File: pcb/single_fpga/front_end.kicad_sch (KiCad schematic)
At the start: 12 parts, among them J1 Main Power Input, J2 AXK5S80347YG, U1 TLV62569DBV

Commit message: Made CON1-4 separate parts. Fixed board-to-board connectors.
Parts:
- J2: value AXK5S80347YG -> AXK5S80337YG; footprint AXK5S80347YG:CONN80_AXK5S80347YG_PAN -> AXK5S80337YG:AXK5S80337YG; symbol AXK5S80347YG:AXK5S80347YG -> AXK5S80337YG:AXK5S80337YG
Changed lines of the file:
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@@
 	)
 	(symbol
-		(lib_id "AXK5S80347YG:AXK5S80347YG")
+		(lib_id "AXK5S80337YG:AXK5S80337YG")
 		(at 219.71 39.37 0)
 		(unit 1)
@@
 			)
 		)
-		(property "Value" "AXK5S80347YG"
+		(property "Value" "AXK5S80337YG"
 			(at 230.378 36.068 0)
 			(show_name no)
@@
 			)
 		)
-		(property "Footprint" "AXK5S80347YG:CONN80_AXK5S80347YG_PAN"
+		(property "Footprint" "AXK5S80337YG:AXK5S80337YG"
 			(at 219.71 39.37 0)
 			(hide yes)
@@
 			)
 		)
-		(property "Datasheet" "https://www.mouser.com/catalog/specsheets/AXK.pdf"
+		(property "Datasheet" "datasheets/con_eng_p5k.pdf"
 			(at 219.71 39.37 0)
 			(hide yes)
@@
 			)
 		)
-		(property "Description" "Panasonic AXK580137YG -- P5K series 0.5mm-pitch 80-pin board-to-board SOCKET, module side (confirmed on the ALINX AC7200 module; mates with the carrier board's own AXK680337YG header -- see ../../AC7200/AC7200_README.md). Real dimensions from Panasonic/Mouser's own P5K/P5KS catalog PDF (mouser.com/catalog/specsheets/AXK.pdf), read directly: body 23.20 x 19.50mm (A x B, same as the header), 0.5mm pitch, 40 pins/row x 2 rows staggered by 0.25mm (half pitch), pad 0.25 x 0.75mm, total footprint span 6.80mm (wider than the header's 5.60mm -- read directly off the Socket's own land-pattern drawing, not assumed equal to the header). Part number CONFIRMED, not assumed: the AC7200 module's own STEP model (AC7200.3.0.stp) names this connector 'AXK680137YG', which doesn't decode against Panasonic's real P5K part-number table (leading digit 6 = Header selector, but mated-height digit 1 is documented Socket-only) -- flagged as a likely STEP-model typo when this part was first built. ALINX's own real schematic (docs/AC7200_Schematic.pdf, page 12 'AC7200 CONNECTOR') settles it: all 4 connector reference labels explicitly read 'AXK580137YG', confirming the STEP model's name was wrong and this (leading digit 5) is the real part. All 320 CON1-4 signal-pin assignments in ../../AC7200/KiCad/AC7200.kicad_sym were also cross-checked pin-by-pin against that same real schematic -- exact match, no discrepancies. Pin numbering on THIS standalone connector symbol (1-80 sequential by row) is still an ASSUMED convention, matching the header's own same assumption -- the real schematic only labels FPGA bank/ball nets on CON1-4, not this connector's own physical pin-to-number layout, so it wasn't independently verifiable against a real pin-1 diagram in the catalog either."
+		(property "Description" "Panasonic AXK5S80337YG -- P5KS 0.5mm-pitch 80-pin board-to-board SOCKET, 7.0/8.0/9.0mm mated height, with positioning bosses. Mates AXK6S80637YG at 9.0mm."
 			(at 219.71 39.37 0)
 			(hide yes)

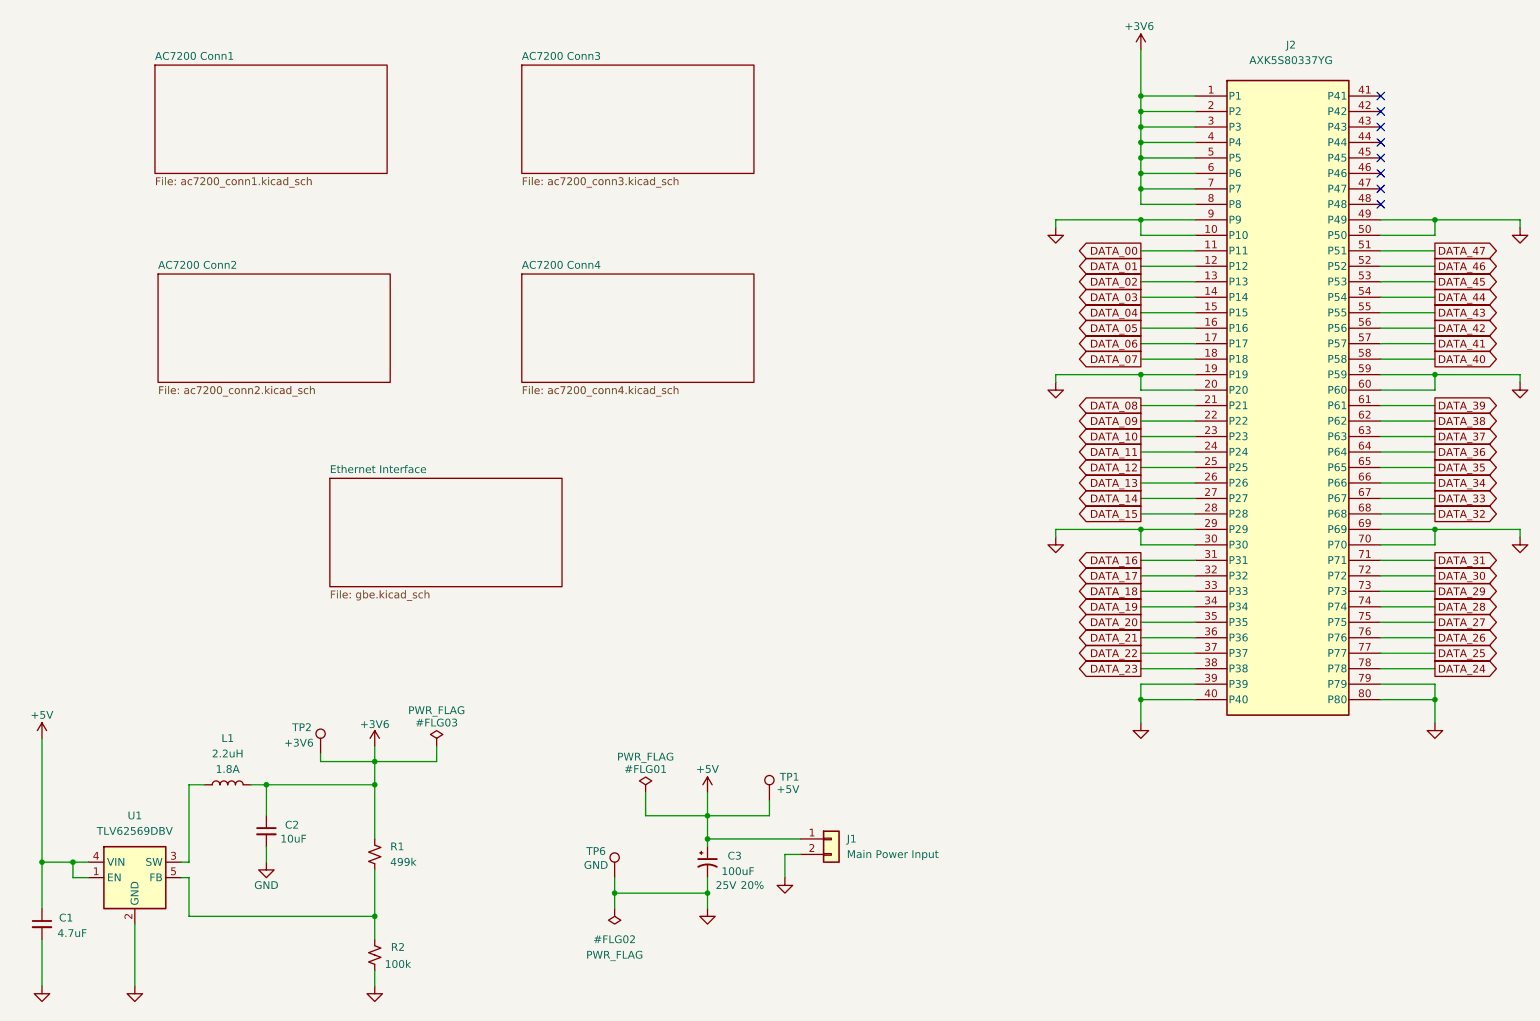
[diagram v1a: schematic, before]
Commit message: Fixed power rails. Fixed C3. Changed U4. ERC FEB.
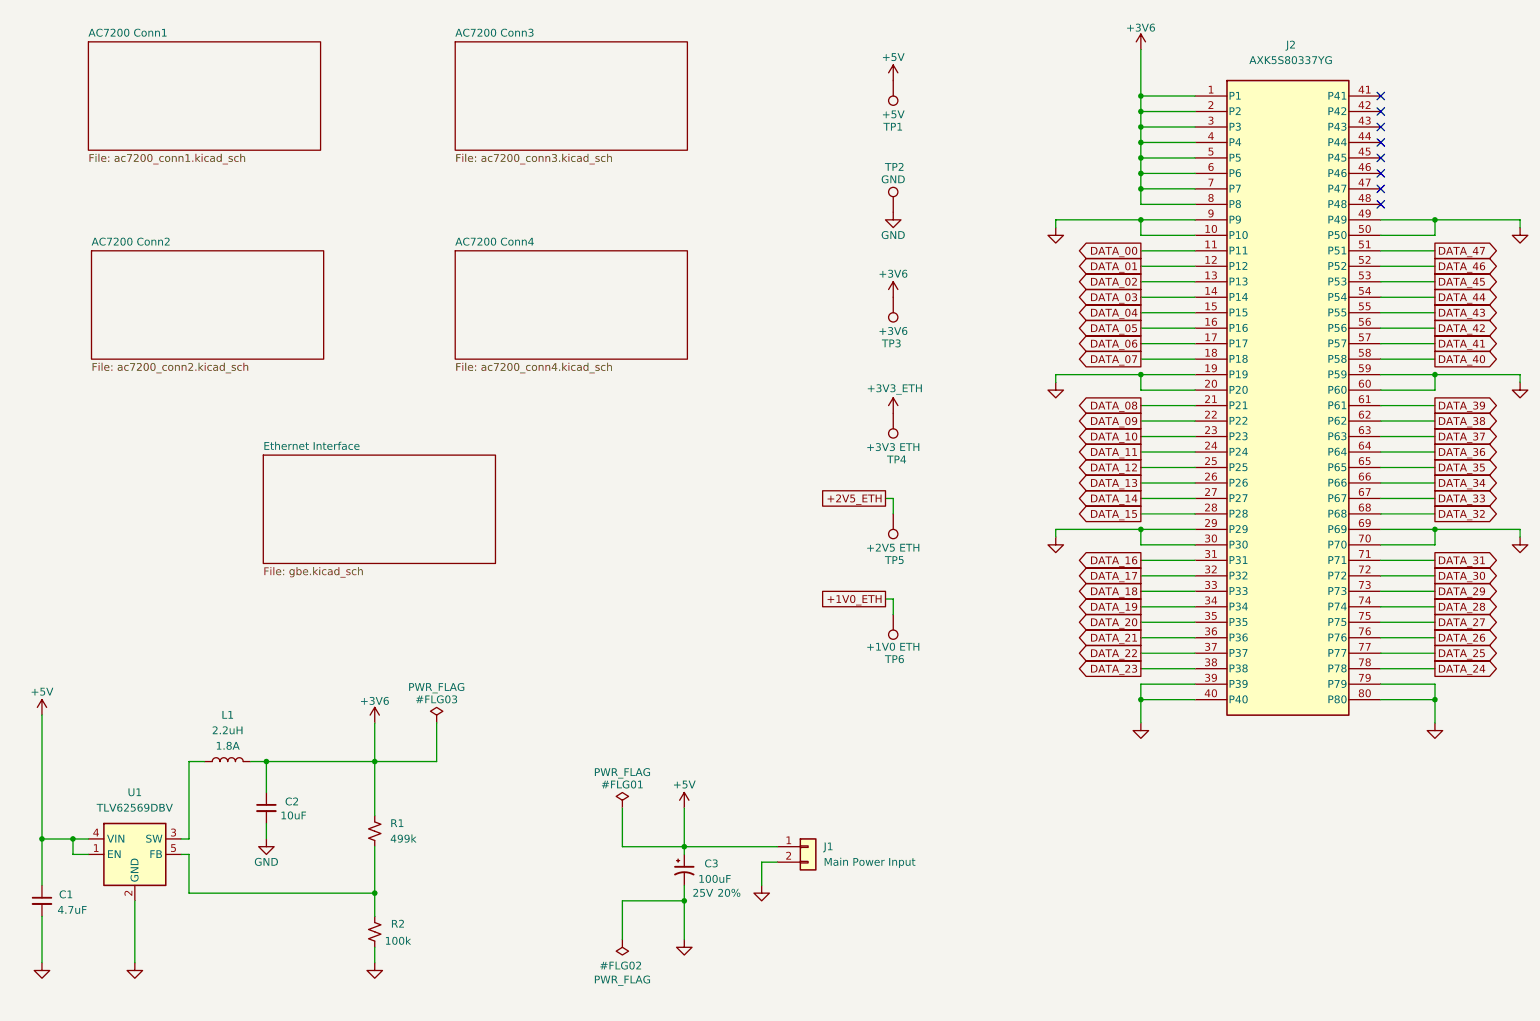
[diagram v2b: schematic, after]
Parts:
- added TP3: +3V6, TestPoint:TestPoint_THTPad_D2.0mm_Drill1.0mm, symbol Connector:TestPoint
- added TP4: +3V3 ETH, TestPoint:TestPoint_THTPad_D2.0mm_Drill1.0mm, symbol Connector:TestPoint
- added TP5: +2V5 ETH, TestPoint:TestPoint_THTPad_D2.0mm_Drill1.0mm, symbol Connector:TestPoint
- C3: footprint PCM_SparkFun-Capacitor:Panasonic_D -> Capacitor_SMD:CP_Elec_6.3x5.8
- TP2: value +3V6 -> GND
- TP6: value GND -> +1V0 ETH
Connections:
- net +3V6: now also TP3.1; no longer TP2.1
- net GND: now also TP2.1; no longer TP6.1
- new net +1V0_ETH: TP6.1
- new net +2V5_ETH: TP5.1
- new net +3V3_ETH: TP4.1
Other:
- moved on the sheet: C1, C2, C3, J1, L1, R1, R2, U1

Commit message: Routed. Almost DRC-clean.
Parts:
- C1: footprint SparkFun-Capacitor:C_1206_3216Metric -> Capacitor_SMD:C_0805_2012Metric; Manufacturer (none) -> Murata; PROD_ID CAP-10300 -> (none); Part Number (none) -> GRM21BR71A475KA73L; Temperature Coefficient Y5V -> X7R; Tolerance (none) -> 10%; Voltage (none) -> 10V
- C2: footprint PCM_SparkFun-Capacitor:C_0805_2012Metric -> Capacitor_SMD:C_0805_2012Metric; Manufacturer (none) -> Murata; PROD_ID CAP-14259 -> (none); Part Number (none) -> GRM21BR71A106KE51L; Temperature Coefficient (none) -> X7R; Tolerance (none) -> 10%; Voltage (none) -> 10V
- L1: footprint Inductor_SMD:L_Taiyo-Yuden_NR-20xx_HandSoldering -> Inductor_SMD:L_Murata_DFE201610P; Manufacturer TDK -> Murata; Manufacturer 2 Taiyo Yuden -> (none); Part Number 2 NRH2412T2R2MNGH -> (none)
- R1, R2: footprint PCM_SparkFun-Resistor:R_0603_1608Metric -> Resistor_SMD:R_0603_1608Metric; PROD_ID RES-07828 -> (none); Tolerance (none) -> 1%
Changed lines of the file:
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@@
 			)
 		)
-		(property "Footprint" "SparkFun-Capacitor:C_1206_3216Metric"
+		(property "Footprint" "Capacitor_SMD:C_0805_2012Metric"
 			(at 25.4 185.42 0)
 			(hide yes)
@@
 			)
 		)
-		(property "Datasheet" "https://search.kemet.com/download/datasheet/C1206C475Z4VAC7800"
+		(property "Datasheet" ""
 			(at 25.4 190.5 0)
 			(hide yes)
@@
 			)
 		)
-		(property "PROD_ID" "CAP-10300"
-			(at 24.13 187.96 0)
-			(hide yes)
-			(show_name no)
-			(do_not_autoplace no)
-			(effects
-				(font
-					(size 1.27 1.27)
-				)
-			)
-		)
-		(property "Voltage" ""
+		(property "Voltage" "10V"
 			(at 27.94 175.2662 0)
 			(hide yes)
@@
 			)
 		)
-		(property "Tolerance" ""
+		(property "Tolerance" "10%"
 			(at 27.94 177.8062 0)
 			(hide yes)
@@
 			)
 		)
-		(property "Temperature Coefficient" "Y5V"
+		(property "Temperature Coefficient" "X7R"
 			(at 26.162 195.834 0)
+			(hide yes)
+			(show_name no)
+			(do_not_autoplace no)
+			(effects
+				(font
+					(size 1.27 1.27)
+				)
+			)
+		)
+		(property "Manufacturer" "Murata"
+			(at 25.4 190.5 0)
+			(hide yes)
+			(show_name no)
+			(do_not_autoplace no)
+			(effects
+				(font
+					(size 1.27 1.27)
+				)
+			)
+		)
+		(property "Part Number" "GRM21BR71A475KA73L"
+			(at 25.4 190.5 0)
 			(hide yes)
 			(show_name no)
@@
 			)
 		)
-		(property "Footprint" "PCM_SparkFun-Resistor:R_0603_1608Metric"
+		(property "Footprint" "Resistor_SMD:R_0603_1608Metric"
 			(at 75.692 162.56 0)
 			(hide yes)
@@
 			)
 		)
-		(property "PROD_ID" "RES-07828"
-			(at 73.66 162.56 0)
+		(property "Tolerance" "1%"
+			(at 71.12 162.56 0)
 			(hide yes)
 			(show_name no)
@@
 			)
 		)
-		(property "Footprint" "PCM_SparkFun-Capacitor:C_0805_2012Metric"
+		(property "Footprint" "Capacitor_SMD:C_0805_2012Metric"
 			(at 62.23 170.18 0)
 			(hide yes)
@@
 			)
 		)
-		(property "Datasheet" "https://mm.digikey.com/Volume0/opasdata/d220001/medias/docus/4888/TMK212BBJ106KG-T_SS.pdf"
+		(property "Datasheet" ""
 			(at 62.23 175.26 0)
 			(hide yes)
@@
 			)
 		)
-		(property "PROD_ID" "CAP-14259"
-			(at 60.96 172.72 0)
-			(hide yes)
-			(show_name no)
-			(do_not_autoplace no)
-			(effects
-				(font
-					(size 1.27 1.27)
-				)
-			)
-		)
-		(property "Voltage" ""
+		(property "Voltage" "10V"
 			(at 64.77 160.0262 0)
 			(hide yes)
@@
 			)
 		)
-		(property "Tolerance" ""
+		(property "Tolerance" "10%"
 			(at 64.77 162.5662 0)
 			(hide yes)
@@
 				)
 				(justify left)
+			)
+		)
+		(property "Manufacturer" "Murata"
+			(at 62.23 175.26 0)
+			(hide yes)
+			(show_name no)
+			(do_not_autoplace no)
+			(effects
+				(font
+					(size 1.27 1.27)
+				)
+			)
+		)
+		(property "Part Number" "GRM21BR71A106KE51L"
+			(at 62.23 175.26 0)
+			(hide yes)
+			(show_name no)
+			(do_not_autoplace no)
+			(effects
+				(font
+					(size 1.27 1.27)
+				)
+			)
+		)
+		(property "Temperature Coefficient" "X7R"
+			(at 62.23 175.26 0)
+			(hide yes)
+			(show_name no)
+			(do_not_autoplace no)
+			(effects
+				(font
+					(size 1.27 1.27)
+				)
 			)
 		)
@@
 			)
 		)
-		(property "Footprint" "Inductor_SMD:L_Taiyo-Yuden_NR-20xx_HandSoldering"
+		(property "Footprint" "Inductor_SMD:L_Murata_DFE201610P"
 			(at 68.58 149.86 0)
 			(hide yes)
@@
 			)
 		)
-		(property "Manufacturer" "TDK"
+		(property "Manufacturer" "Murata"
 			(at 65.278 153.67 0)
 			(hide yes)
@@
 		(property "Display 2" "1.8A"
 			(at 55.88 148.59 90)
-			(show_name no)
-			(do_not_autoplace no)
-			(effects
-				(font
-					(size 1.27 1.27)
-				)
-			)
-		)
-		(property "Part Number 2" "NRH2412T2R2MNGH"
-			(at 55.88 151.13 0)
-			(hide yes)
-			(show_name no)
-			(do_not_autoplace no)
-			(effects
-				(font
-					(size 1.27 1.27)
-				)
-			)
-		)
-		(property "Manufacturer 2" "Taiyo Yuden"
-			(at 55.88 151.13 0)
-			(hide yes)
 			(show_name no)
 			(do_not_autoplace no)
@@
 			)
 		)
-		(property "Footprint" "PCM_SparkFun-Resistor:R_0603_1608Metric"
+		(property "Footprint" "Resistor_SMD:R_0603_1608Metric"
 			(at 84.328 179.07 0)
 			(hide yes)
@@
 			)
 		)
-		(property "PROD_ID" "RES-07828"
-			(at 86.36 179.07 0)
-			(hide yes)
-			(show_name no)
+		(property "Tolerance" "1%"
+			(at 88.9 179.07 0)
+			(hide yes)
+			(show_name no)

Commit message: Added TXCO divide by FPGA.
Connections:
- net GND: now also J2.43 (P43)
- net TCXO_CLK: now reaches J2.41 (P41)
- net PDM_CLK: now reaches J2.45 (P45)
- no-connect marks 8 -> 5
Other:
- moved on the sheet: TP1, TP2, TP3, TP4, TP5, TP6

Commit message: Fixed thermal pad. Moved RGMII lines to be in the same bank.
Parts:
- added TP7: TCXO CLK, TestPoint:TestPoint_THTPad_D2.0mm_Drill1.0mm, symbol Connector:TestPoint
- added TP8: PDM CLK, TestPoint:TestPoint_THTPad_D2.0mm_Drill1.0mm, symbol Connector:TestPoint
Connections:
- net PDM_CLK: now also TP8.1
- net TCXO_CLK: now also TP7.1

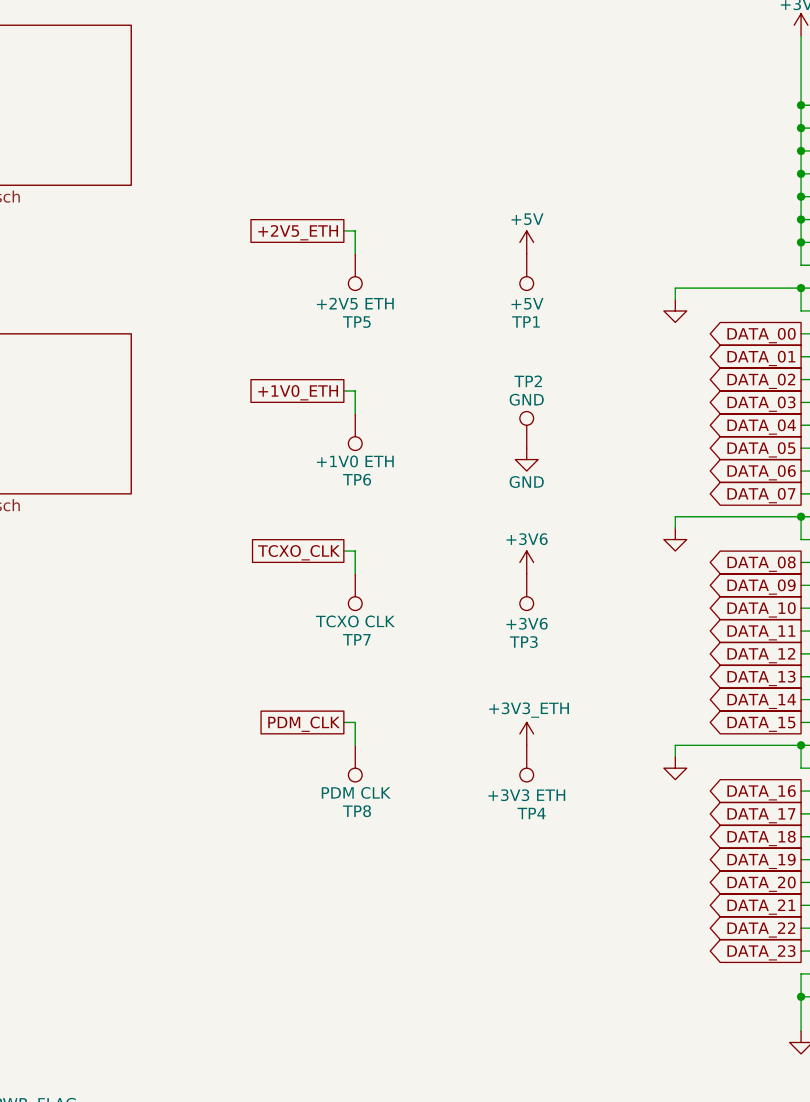
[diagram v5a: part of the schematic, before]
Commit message: Added more GND test points.
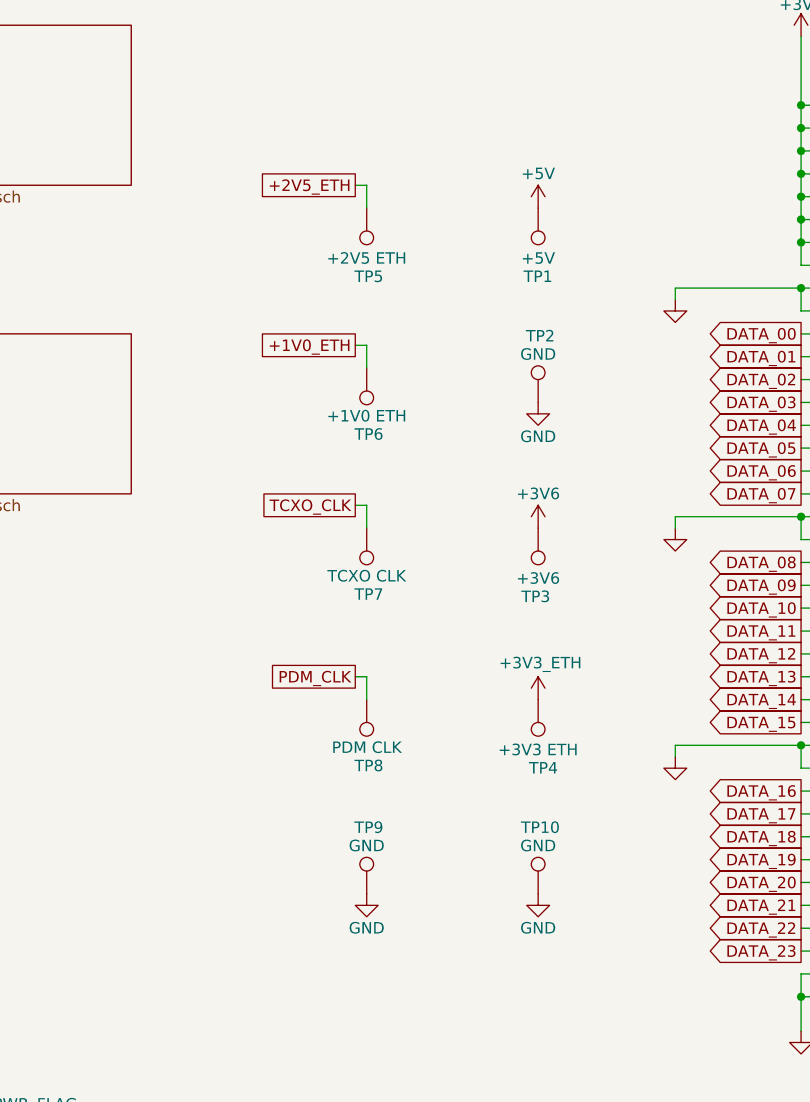
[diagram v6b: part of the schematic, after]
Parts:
- added TP10, TP9: GND, TestPoint:TestPoint_THTPad_D2.0mm_Drill1.0mm, symbol Connector:TestPoint
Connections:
- net GND: now also TP10.1, TP9.1
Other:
- moved on the sheet: TP1, TP2, TP3, TP4, TP5, TP6, TP7, TP8
